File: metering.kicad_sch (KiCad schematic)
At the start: 43 parts, among them J1 Conn_01x08, J2 USB_C_Receptacle_USB2.0_16P, J3 Prog, P1 Conn_01x08, SW1 Reset, SW2 Boot, U1 USBLC6-2SC6, U2 AMS1117-3.3, U3 ESP32-C3-WROOM-02U, U4 74HC14, X1 Screw_Terminal_01x06, X2 Screw_Terminal_01x06, Y1 32.768kHz

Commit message: Update to KiCad 10
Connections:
- net GND: now also J2.SH (SHIELD); no longer J2.S1 (SHIELD)

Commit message: Clear PCB and prepare layout for CNMB-3-2
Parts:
- H1, H2: footprint MountingHole:MountingHole_3.2mm_M3 -> MountingHole:MountingHole_4.3mm_M4
- X1: renamed from X2; footprint TerminalBlock_Phoenix:TerminalBlock_Phoenix_MKDS-1,5-6-5.08_1x06_P5.08mm_Horizontal -> TerminalBlock_Phoenix:TerminalBlock_Phoenix_MKDS-1,5-9-5.08_1x09_P5.08mm_Horizontal; symbol Connector:Screw_Terminal_01x06 -> Connector:Screw_Terminal_01x09
- X2: renamed from X1; footprint TerminalBlock_Phoenix:TerminalBlock_Phoenix_MKDS-1,5-6-5.08_1x06_P5.08mm_Horizontal -> TerminalBlock_Phoenix:TerminalBlock_Phoenix_MKDS-1,5-9-5.08_1x09_P5.08mm_Horizontal; symbol Connector:Screw_Terminal_01x06 -> Connector:Screw_Terminal_01x09
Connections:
- net GND1: no longer X1.1 (Pin_1), X1.3 (Pin_3), X1.5 (Pin_5), X2.2 (Pin_2), X2.3 (Pin_3)
- net at X1.2 (Pin_2): no longer J1.8 (Pin_8)
- net at X1.4 (Pin_4): no longer J1.7 (Pin_7)
- net at X1.6 (Pin_6): no longer J1.6 (Pin_6)
- net at J1.2 (Pin_2): no longer X2.1 (Pin_1)
- net at J1.3 (Pin_3): no longer X2.4 (Pin_4)
- net at J1.4 (Pin_4): no longer X2.5 (Pin_5)
- net at J1.5 (Pin_5): no longer X2.6 (Pin_6)
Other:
- title: Smart Home Energy Metering -> Smart Home Metering
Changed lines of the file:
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@@
 	(paper "A4")
 	(title_block
-		(title "Smart Home Energy Metering")
-		(date "2025-08-01")
+		(title "Smart Home Metering")
+		(date "2026-09-20")
 		(rev "1.2")
 		(comment 1 "https://github.com/zargony/smarthome-metering")
@@
 	)
 	(symbol
-		(lib_id "Connector:Screw_Terminal_01x06")
-		(at 69.85 68.58 0)
+		(lib_id "Connector:Screw_Terminal_01x09")
+		(at 68.58 73.66 0)
 		(mirror y)
 		(unit 1)
@@
 		(in_pos_files yes)
 		(dnp no)
-		(property "Reference" "X2"
-			(at 69.85 57.15 0)
+		(property "Reference" "X1"
+			(at 68.58 57.15 0)
 			(show_name no)
 			(do_not_autoplace no)
@@
 		)
 		(property "Value" "Screw_Terminal_01x06"
-			(at 69.85 59.69 0)
+			(at 68.58 59.69 0)
 			(show_name no)
 			(do_not_autoplace no)
@@
 			)
 		)
-		(property "Footprint" "TerminalBlock_Phoenix:TerminalBlock_Phoenix_MKDS-1,5-6-5.08_1x06_P5.08mm_Horizontal"
-			(at 69.85 68.58 0)
+		(property "Footprint" "TerminalBlock_Phoenix:TerminalBlock_Phoenix_MKDS-1,5-9-5.08_1x09_P5.08mm_Horizontal"
+			(at 68.58 73.66 0)
 			(hide yes)
 			(show_name no)
@@
 		)
 		(property "Datasheet" ""
-			(at 69.85 68.58 0)
+			(at 68.58 73.66 0)
 			(hide yes)
 			(show_name no)
@@
 			)
 		)
-		(property "Description" "Generic screw terminal, single row, 01x06, script generated (kicad-library-utils/schlib/autogen/connector/)"
-			(at 69.85 68.58 0)
+		(property "Description" "Generic screw terminal, single row, 01x09, script generated (kicad-library-utils/schlib/autogen/connector/)"
+			(at 68.58 73.66 0)
 			(hide yes)
 			(show_name no)
@@
 		(pin "6"
 		)
+		(pin "8"
+		)
+		(pin "9"
+		)
+		(pin "7"
+		)
 		(instances
 			(project "metering"
 				(path "/2132c704-8b90-4a68-a04d-0b4be367d67b"
-					(reference "X2")
+					(reference "X1")
 					(unit 1)
 				)
@@
 			)
 		)
-		(property "Footprint" "MountingHole:MountingHole_3.2mm_M3"
+		(property "Footprint" "MountingHole:MountingHole_4.3mm_M4"
 			(at 19.05 190.5 0)
 			(hide yes)
@@
 			)
 		)
-		(property "Footprint" "MountingHole:MountingHole_3.2mm_M3"
+		(property "Footprint" "MountingHole:MountingHole_4.3mm_M4"
 			(at 19.05 184.15 0)
 			(hide yes)
@@
 	)
 	(symbol
-		(lib_id "Connector:Screw_Terminal_01x06")
-		(at 69.85 43.18 0)
+		(lib_id "Connector:Screw_Terminal_01x09")
+		(at 68.58 48.26 0)
 		(mirror y)
 		(unit 1)
@@
 		(in_pos_files yes)
 		(dnp no)
-		(property "Reference" "X1"
-			(at 69.85 31.75 0)
+		(property "Reference" "X2"
+			(at 68.58 31.75 0)
 			(show_name no)
 			(do_not_autoplace no)
@@
 		)
 		(property "Value" "Screw_Terminal_01x06"
-			(at 69.85 34.29 0)
+			(at 68.58 34.29 0)
 			(show_name no)
 			(do_not_autoplace no)
@@
 			)
 		)
-		(property "Footprint" "TerminalBlock_Phoenix:TerminalBlock_Phoenix_MKDS-1,5-6-5.08_1x06_P5.08mm_Horizontal"
-			(at 69.85 43.18 0)
+		(property "Footprint" "TerminalBlock_Phoenix:TerminalBlock_Phoenix_MKDS-1,5-9-5.08_1x09_P5.08mm_Horizontal"
+			(at 68.58 48.26 0)
 			(hide yes)
 			(show_name no)
@@
 		)
 		(property "Datasheet" ""
-			(at 69.85 43.18 0)
+			(at 68.58 48.26 0)
 			(hide yes)
 			(show_name no)
@@
 			)
 		)
-		(property "Description" "Generic screw terminal, single row, 01x06, script generated (kicad-library-utils/schlib/autogen/connector/)"
-			(at 69.85 43.18 0)
+		(property "Description" "Generic screw terminal, single row, 01x09, script generated (kicad-library-utils/schlib/autogen/connector/)"
+			(at 68.58 48.26 0)
 			(hide yes)
 			(show_name no)
@@
 		(pin "3"
 		)
+		(pin "7"
+		)
+		(pin "8"
+		)
+		(pin "9"
+		)
 		(instances
 			(project "metering"
 				(path "/2132c704-8b90-4a68-a04d-0b4be367d67b"
-					(reference "X1")
+					(reference "X2")
 					(unit 1)
 				)

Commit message: Rework power supply and screw terminal connections
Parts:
- removed J1: Conn_01x08, Connector_PinSocket_2.54mm:PinSocket_1x08_P2.54mm_Vertical, symbol Connector_Generic:Conn_01x08
- removed P1: Conn_01x08, Connector_PinHeader_2.54mm:PinHeader_1x08_P2.54mm_Horizontal, symbol Connector_Generic:Conn_01x08
- removed U2: AMS1117-3.3, Package_TO_SOT_SMD:SOT-223-3_TabPin2, symbol Regulator_Linear:AMS1117-3.3
- added C14: 100n, Capacitor_SMD:C_0805_2012Metric, symbol Device:C
- added L1: 10u, Inductor_SMD:L_7.3x7.3_H4.5, symbol Device:L
- added R24: 69k8/1%, Resistor_SMD:R_0805_2012Metric, symbol Device:R
- added R25: 22k1/1%, Resistor_SMD:R_0805_2012Metric, symbol Device:R
- added U2: LMR54410FDBVR, Package_TO_SOT_SMD:SOT-23-6, symbol Regulator_Switching:LMR50410
- C1: value 10u -> 2.2u/50V; footprint Capacitor_Tantalum_SMD:CP_EIA-3216-18_Kemet-A -> Capacitor_SMD:C_0805_2012Metric; symbol Device:C_Polarized -> Device:C
- C2: footprint Capacitor_Tantalum_SMD:CP_EIA-3216-18_Kemet-A -> Capacitor_SMD:C_0805_2012Metric; symbol Device:C_Polarized -> Device:C
- D1, D2: value SS12 -> SS14; symbol Diode:SS12 -> Diode:SS14
- X1, X2: value Screw_Terminal_01x06 -> Screw_Terminal_01x09
- renumbered J2 to J1
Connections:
- net +3.3V: now also L1.2, R24.1
- net GND: now also X1.1 (Pin_1), X1.4 (Pin_4), X1.8 (Pin_8), X2.3 (Pin_3), X2.9 (Pin_9), R25.2, U2.2 (GND)
- net UART_RX: now also X1.5 (Pin_5)
- net UART_TX: now also X1.6 (Pin_6)
- net VIN: now also X1.9 (Pin_9)
- net AI2: now reaches X1.2 (Pin_2)
- net AI1: now reaches X1.3 (Pin_3)
- net DI1: now reaches X2.1 (Pin_1)
- net DI2: now reaches X2.2 (Pin_2)
- net DO1: now reaches X2.7 (Pin_7)
- net DO2: now reaches X2.8 (Pin_8)
- net +5V: no longer names the net of C1.1, D1.1 (K), D2.1 (K)
- net +5V: now also U2.4 (EN), U2.5 (VIN)
- new net: C14.1, U2.1 (CB)
- new net: R24.2, R25.1, U2.3 (FB)
- new net: C14.2, L1.1, U2.6 (SW)
- no-connect marks 5 -> 9
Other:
- note added: "5-36V"
- note added: "5V"
- note added: "Analog Inputs"
- note added: "Digital Inputs"
- note added: "Outputs"
- note added: "Power Supply"
- note added: "Serial"
- note added: "use high quality capacitors (X7R)"
- note removed: "3.3V Regulator"
- note removed: "Pulse contacts (e.g. gas/water meter reed contacts)"
- note removed: "UART (e.g. electric meter IR adapter)"
- moved on the sheet: D1, D2, J1, J3, R1, R2, U1, X1, X2

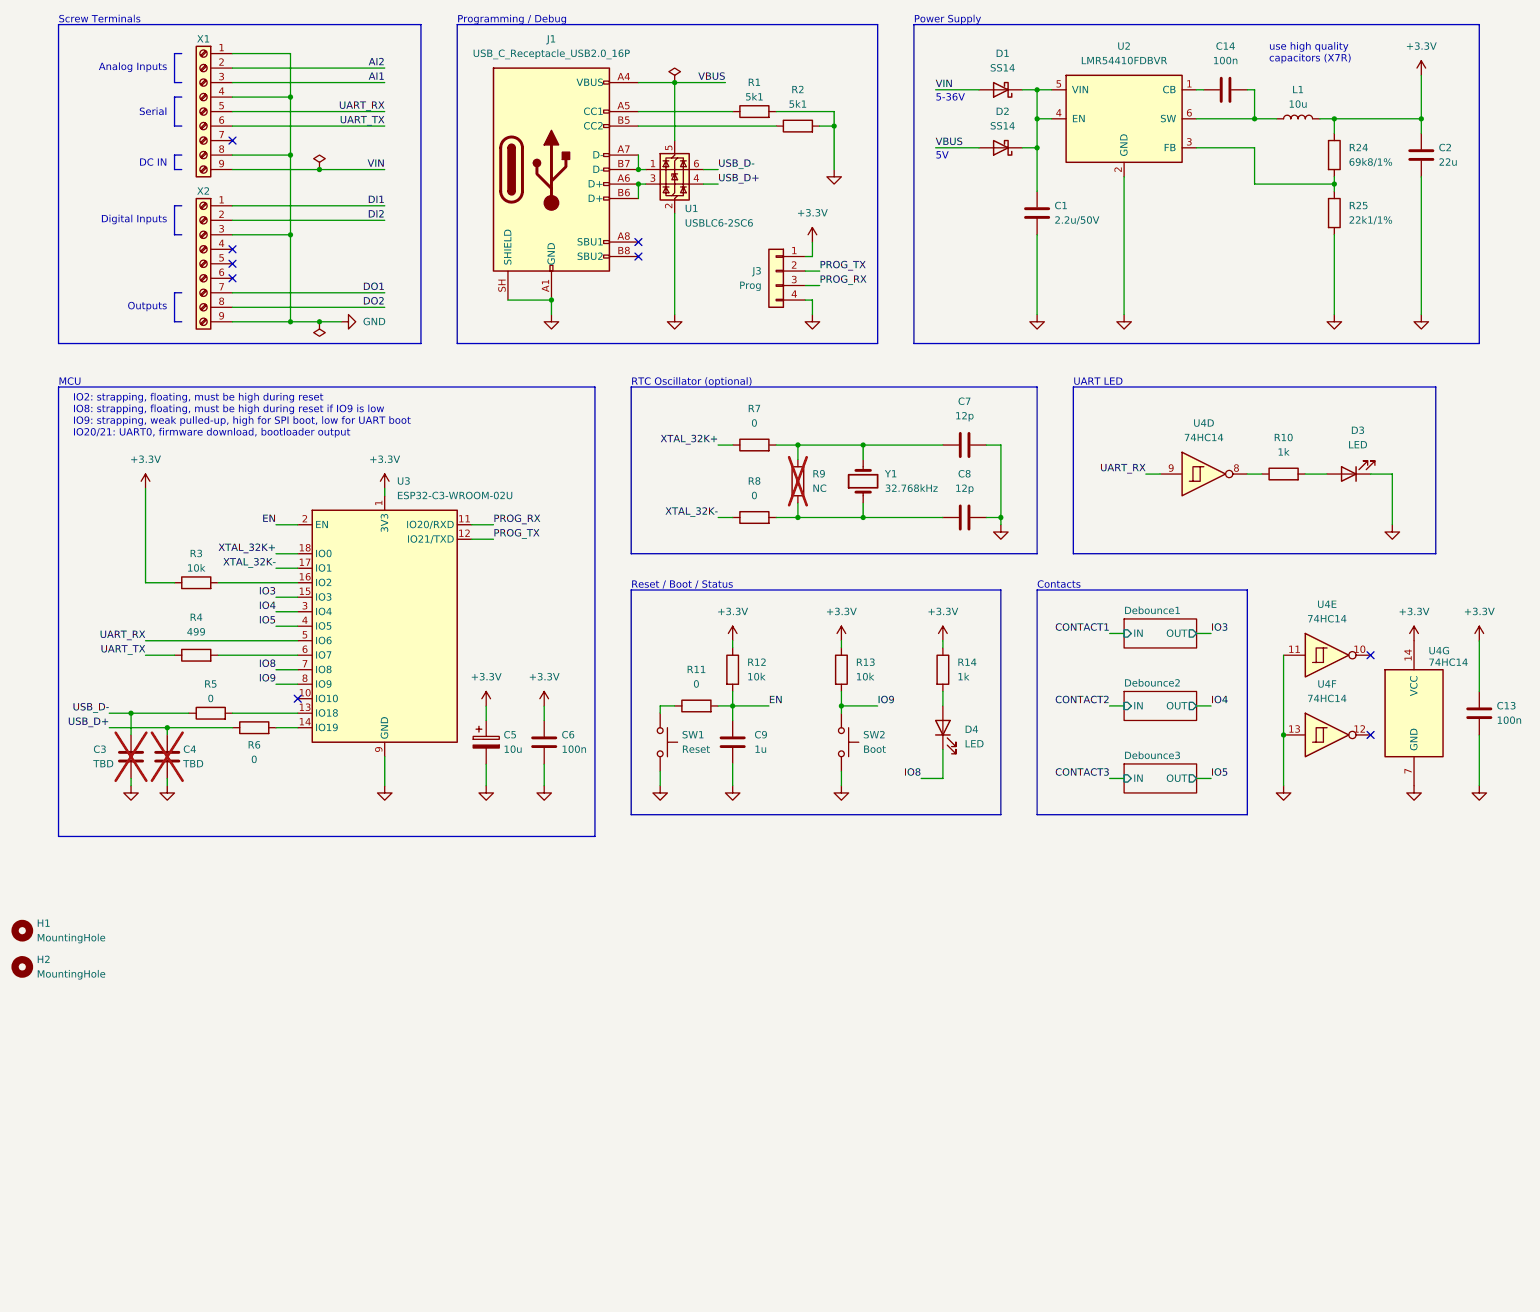
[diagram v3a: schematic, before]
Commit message: Rework digital inputs, add analog inputs and digital outputs
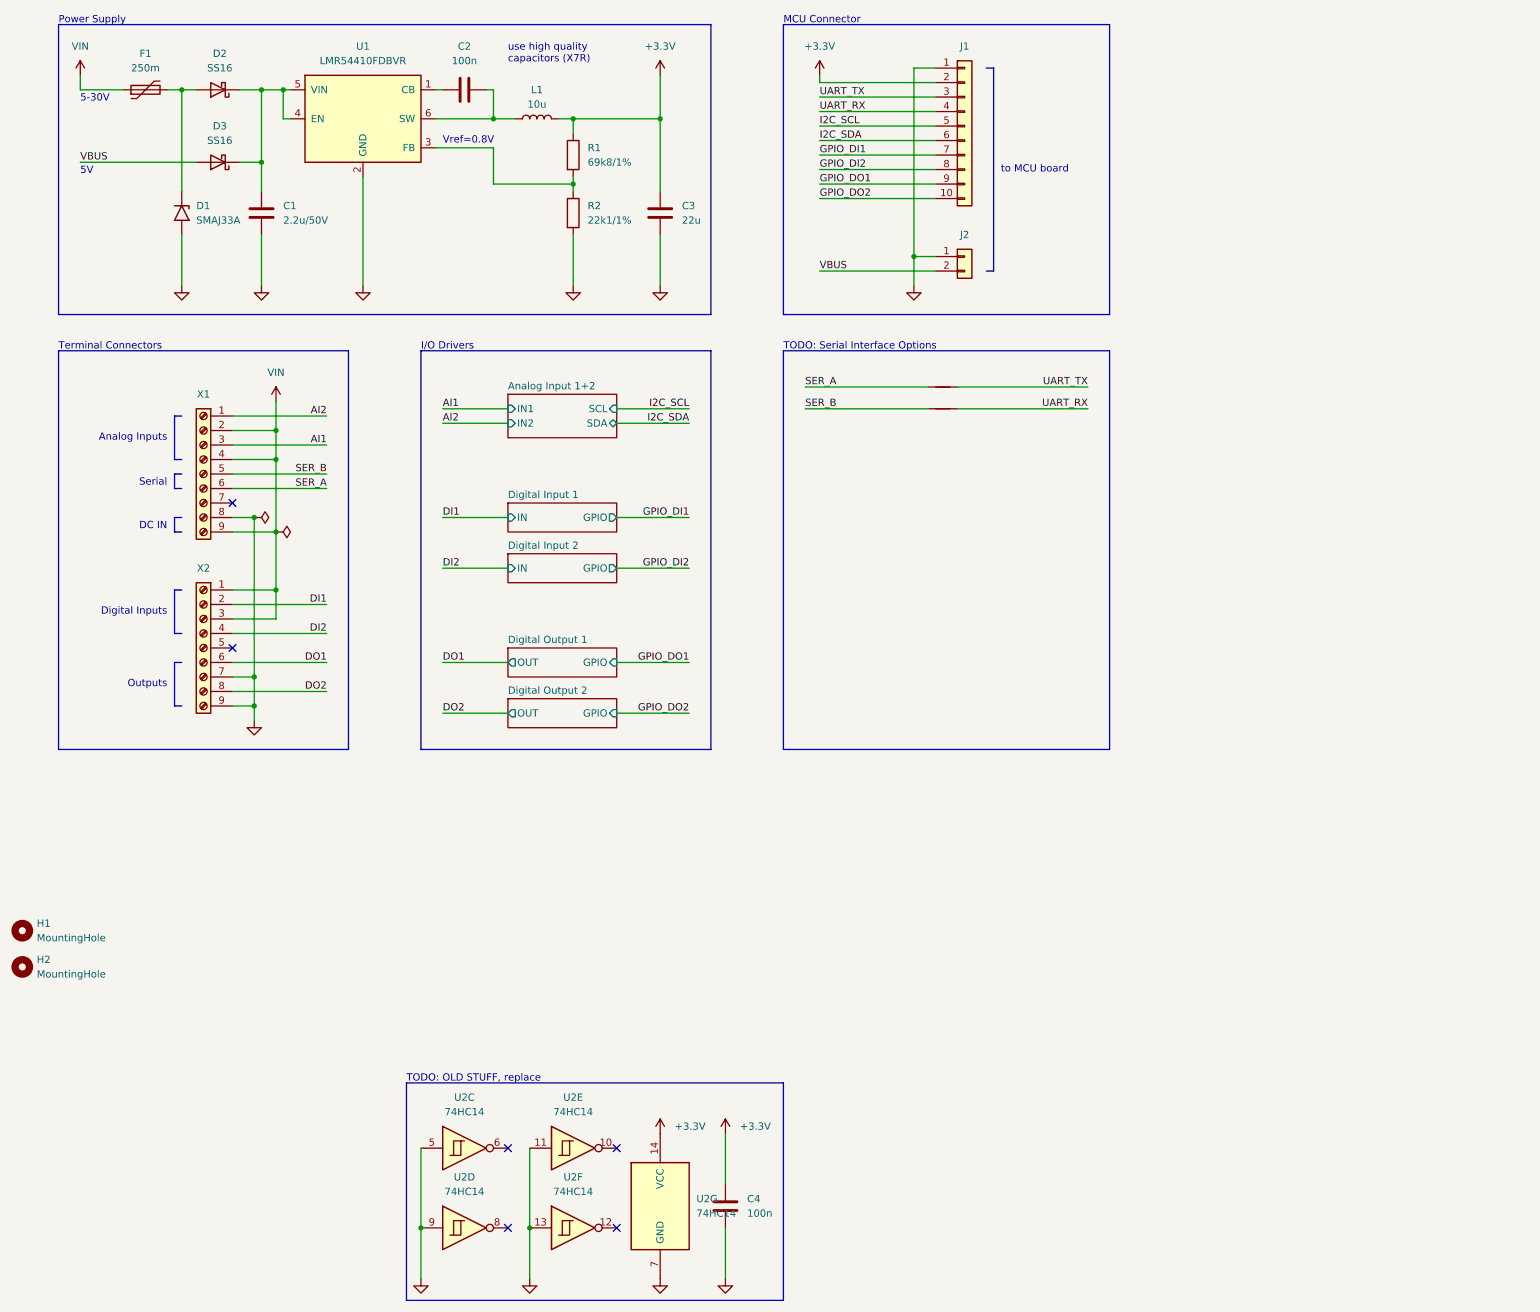
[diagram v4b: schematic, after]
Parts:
- removed C3, C4: TBD, Capacitor_SMD:C_0805_2012Metric, symbol Device:C
- removed C5: 10u, Capacitor_Tantalum_SMD:CP_EIA-3216-18_Kemet-A, symbol Device:C_Polarized
- removed C6: 100n, Capacitor_SMD:C_0805_2012Metric, symbol Device:C
- removed C7, C8: 12p, Capacitor_SMD:C_0805_2012Metric, symbol Device:C
- removed C9: 1u, Capacitor_SMD:C_0805_2012Metric, symbol Device:C
- removed D3, D4: LED, LED_THT:LED_D3.0mm, symbol Device:LED
- removed J1: USB_C_Receptacle_USB2.0_16P, Connector_USB:USB_C_Receptacle_GCT_USB4110, symbol Connector:USB_C_Receptacle_USB2.0_16P
- removed J3: Prog, Connector_PinHeader_2.54mm:PinHeader_1x04_P2.54mm_Vertical, symbol Connector_Generic:Conn_01x04
- removed R1, R2: 5k1, Resistor_SMD:R_0805_2012Metric, symbol Device:R
- removed R10, R14: 1k, Resistor_SMD:R_0805_2012Metric, symbol Device:R
- removed R11, R5, R6, R7, R8: 0, Resistor_SMD:R_0805_2012Metric, symbol Device:R
- removed R12, R13, R3: 10k, Resistor_SMD:R_0805_2012Metric, symbol Device:R
- removed R4: 499, Resistor_SMD:R_0805_2012Metric, symbol Device:R
- removed R9: NC, Resistor_SMD:R_0805_2012Metric, symbol Device:R
- removed SW1: Reset, Button_Switch_SMD:SW_Tactile_SPST_NO_Straight_CK_PTS636Sx25SMTRLFS, symbol Switch:SW_Push
- removed SW2: Boot, Button_Switch_SMD:SW_Tactile_SPST_NO_Straight_CK_PTS636Sx25SMTRLFS, symbol Switch:SW_Push
- removed U1: USBLC6-2SC6, Package_TO_SOT_SMD:SOT-23-6, symbol Power_Protection:USBLC6-2SC6
- removed U3: ESP32-C3-WROOM-02U, RF_Module:ESP32-C3-WROOM-02U, symbol RF_Module:ESP32-C3-WROOM-02
- removed unit 4 of U4
- removed Y1: 32.768kHz, Crystal:Crystal_SMD_3215-2Pin_3.2x1.5mm, symbol Device:Crystal
- added D1: SMAJ33A, Diode_SMD:D_SMA, symbol Diode:SMAJ33A
- added F1: 250m, Fuse:Fuse_1210_3225Metric, symbol Device:Polyfuse
- added J1: Conn_01x10, Connector_JST:JST_PH_B9B-PH-SM4-TB_1x09-1MP_P2.00mm_Vertical, symbol Connector_Generic:Conn_01x10
- added J2: Conn_01x02, Connector_JST:JST_PH_B2B-PH-K_1x02_P2.00mm_Vertical, symbol Connector_Generic:Conn_01x02
- added NT1, NT2: NetTie_2, NetTie:NetTie-2_SMD_Pad0.5mm, symbol Device:NetTie_2
- added unit 3 of U2
- added unit 4 of U2
- C1: footprint Capacitor_SMD:C_0805_2012Metric -> Capacitor_SMD:C_1206_3216Metric
- C3: renamed from C2; footprint Capacitor_SMD:C_0805_2012Metric -> Capacitor_SMD:C_1206_3216Metric
- D2: renamed from D1; value SS14 -> SS16; symbol Diode:SS14 -> Diode:SS16
- D3: renamed from D2; value SS14 -> SS16; symbol Diode:SS14 -> Diode:SS16
- L1: footprint Inductor_SMD:L_7.3x7.3_H4.5 -> Inductor_SMD:L_APV_APH0630
- renumbered C14 to C2, C13 to C4, R24 to R1, R25 to R2, U2 to U1, U4 to U2
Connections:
- net +3.3V: now also J1.2 (Pin_2)
- net AI2: now also X1.1 (Pin_1); no longer X1.2 (Pin_2)
- net DI1: now also X2.2 (Pin_2); no longer X2.1 (Pin_1)
- net DI2: now also X2.4 (Pin_4); no longer X2.2 (Pin_2)
- net DO1: now also X2.6 (Pin_6); no longer X2.7 (Pin_7)
- net GND: now also X2.7 (Pin_7), D1.2 (A2), J1.1 (Pin_1), J2.1 (Pin_1), U2.5, U2.9; no longer X1.1 (Pin_1), X1.4 (Pin_4), X2.3 (Pin_3)
- net UART_RX: now also J1.4 (Pin_4), NT2.2; no longer X1.5 (Pin_5)
- net UART_TX: now also J1.3 (Pin_3), NT1.2; no longer X1.6 (Pin_6)
- net VBUS: now also J2.2 (Pin_2)
- net VIN: now also X1.2 (Pin_2), X1.4 (Pin_4), X2.1 (Pin_1), X2.3 (Pin_3), F1.1; no longer D2.2 (A)
- new net: D1.1 (A1), D2.2 (A), F1.2
- new net GPIO_DI1: J1.7 (Pin_7)
- new net GPIO_DI2: J1.8 (Pin_8)
- new net GPIO_DO1: J1.9 (Pin_9)
- new net GPIO_DO2: J1.10 (Pin_10)
- new net I2C_SCL: J1.5 (Pin_5)
- new net I2C_SDA: J1.6 (Pin_6)
- new net SER_A: NT1.1, X1.6 (Pin_6)
- new net SER_B: NT2.1, X1.5 (Pin_5)
- no-connect marks 9 -> 6
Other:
- removed sheet Debounce1
- removed sheet Debounce2
- removed sheet Debounce3
- added sheet Analog Input 1+2 (analog-in.kicad_sch)
- added sheet Digital Input 1 (digital-in.kicad_sch)
- added sheet Digital Input 2 (digital-in.kicad_sch)
- added sheet Digital Output 1 (digital-out.kicad_sch)
- added sheet Digital Output 2 (digital-out.kicad_sch)
- note added: "5-30V"
- note added: "I/O Drivers"
- note added: "MCU Connector"
- note added: "TODO: OLD STUFF, replace"
- note added: "TODO: Serial Interface Options"
- note added: "Terminal Connectors"
- note added: "Vref=0.8V"
- note added: "to MCU board"
- note removed: "5-36V"
- note removed: "Contacts"
- note removed: "IO2: strapping, floating, must be high during reset IO8: strapping, floating, must be high during reset if IO9 is low IO9: strapping, weak pulled-up, high for SPI boot, low for UART boot IO20/21: UART0, firmware download, bootloader output"
- note removed: "MCU"
- note removed: "Programming / Debug"
- note removed: "RTC Oscillator (optional)"
- note removed: "Reset / Boot / Status"
- note removed: "Screw Terminals"
- note removed: "UART LED"
- moved on the sheet: C1, C2, C3, C4, D2, D3, L1, R1, R2, U1, U2E, U2F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
